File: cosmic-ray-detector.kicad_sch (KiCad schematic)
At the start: 51 parts, among them J1 15-91-0060, J2 15-91-0060, J3 SJ-43515RS-SMT, U1 LT3461, U2 LT1807, U3 Arduino_Nano_v3.x

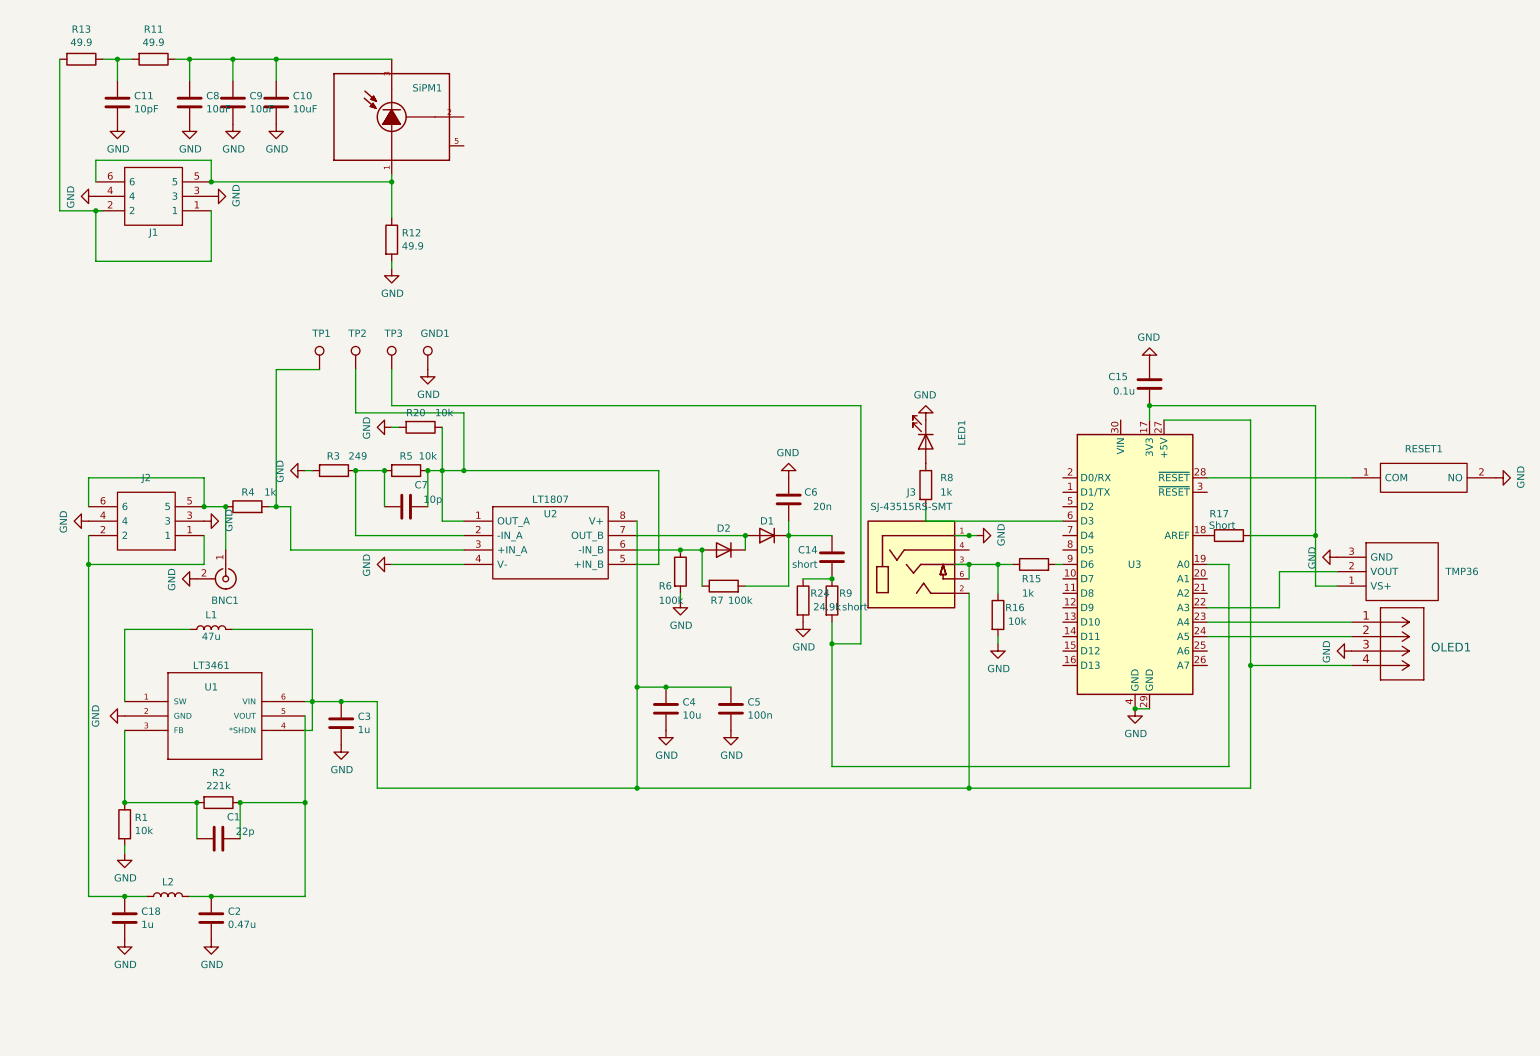
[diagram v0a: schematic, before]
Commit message: Add KiCad PCB project, CAD models, gerbers, libraries, and outputs
Track the full hardware project: KiCad schematic/PCB sources (v2 and
split variants), component libraries and 3D shapes, fabrication outputs
(gerbers, drill, position/BOM CSVs, STEP/STL/WRL), CAD enclosure models,
schematic exports (SVG/PDF), SPICE models, and reference photos.

Co-Authored-By: Claude Opus 4.8 <noreply@anthropic.com>
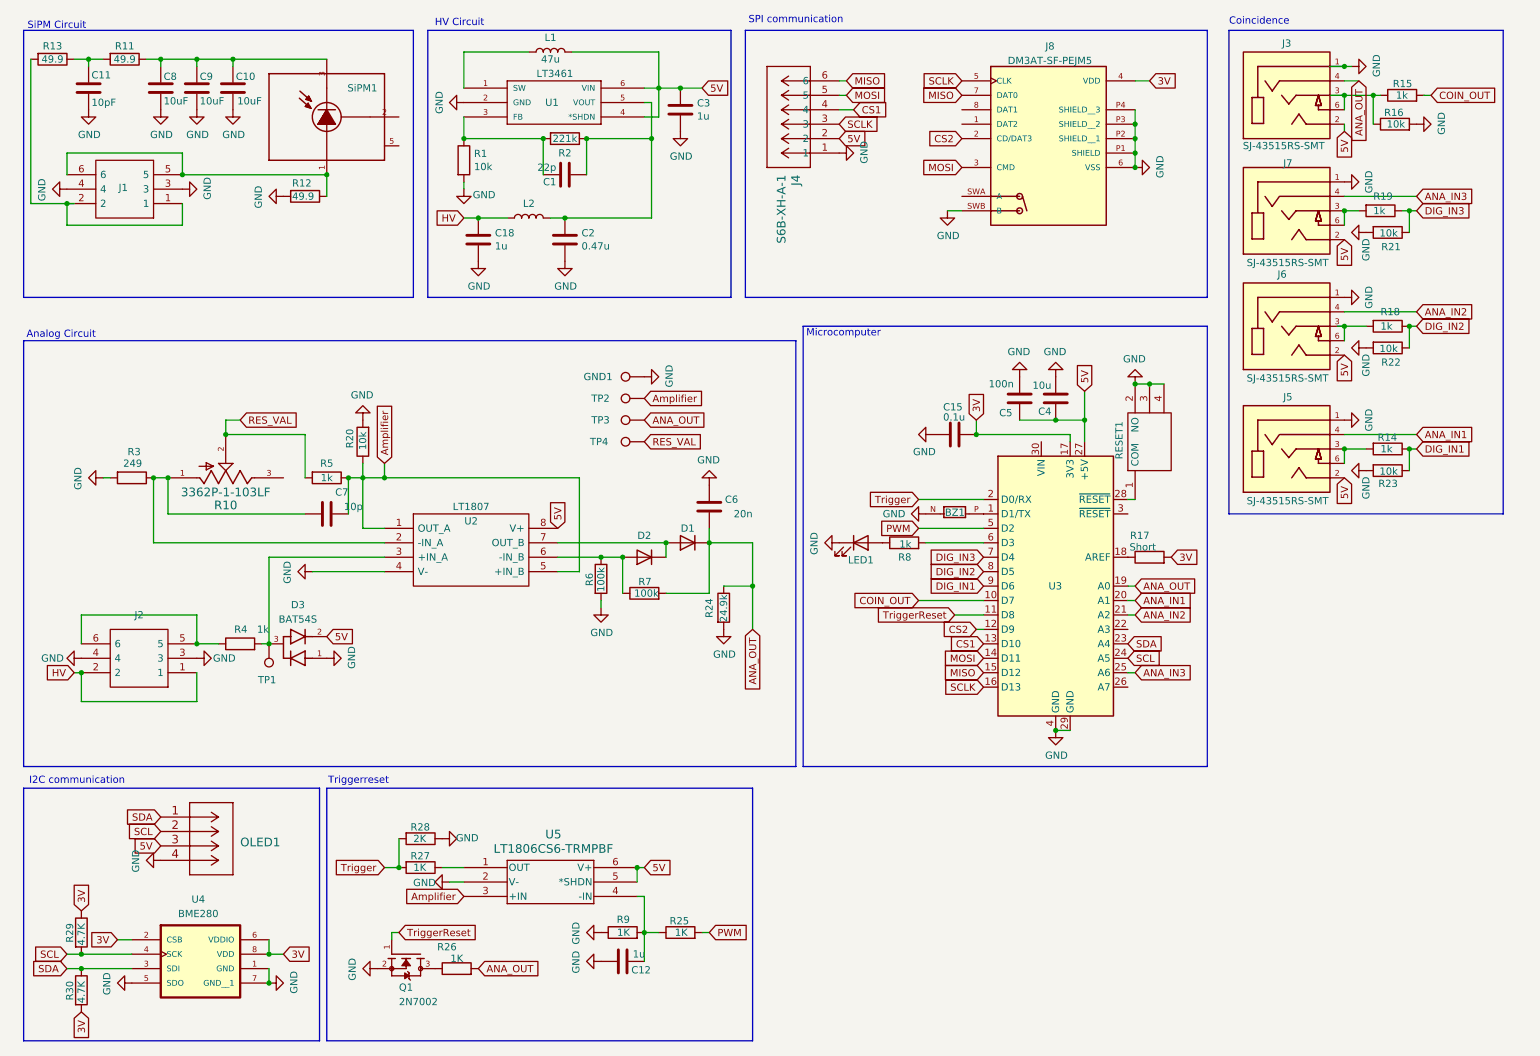
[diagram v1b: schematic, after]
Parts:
- removed BNC1: Conn_Coaxial, Connector_Coaxial:BNC_Amphenol_B6252HB-NPP3G-50_Horizontal, symbol Connector:Conn_Coaxial
- removed C14: short, Capacitor_SMD:C_0805_2012Metric, symbol Device:C
- removed TMP36: TMP36GT9Z, SamacSys_Parts:TO-92, symbol SamacSys_Parts:TMP36GT9Z
- added BZ1: CPT-1117-83-SMT-TR, SamacSys_Parts:XDCR_CPT-1117-83-SMT-TR, symbol CPT-1117-83-SMT-TR:CPT-1117-83-SMT-TR
- added C12: 1u, Capacitor_SMD:C_0805_2012Metric, symbol Device:C
- added D3: BAT54S, SamacSys_Parts:SOT95P240X120-3N, symbol cosmic-ray-detector:BAT54S
- added J4: S6B-XH-A-1, CONN_S6B-XH-A-1_JST, symbol cosmic-ray-detector:S6B-XH-A-1
- added J5, J6, J7: SJ-43515RS-SMT, cosmic-ray-detector:SJ-43515RS-SMT-TR, symbol SJ-43515RS-SMT:SJ-43515RS-SMT
- added J8: DM3AT-SF-PEJM5, cosmic-ray-detector:HRS_DM3AT-SF-PEJM5, symbol DM3AT-SF-PEJM5:DM3AT-SF-PEJM5
- added Q1: 2N7002, SamacSys_Parts:SOT95P240X111-3N, symbol cosmic-ray-detector:2N7002
- added R10: 3362P-1-103LF, SamacSys_Parts:TRIM_3362P-1-103LF, symbol cosmic-ray-detector:3362P-1-103LF
- added R14, R18, R19: 1k, Resistor_SMD:R_0805_2012Metric, symbol Device:R
- added R21, R22, R23: 10k, Resistor_SMD:R_0805_2012Metric, symbol Device:R
- added R25, R26, R27: 1K, Resistor_SMD:R_0805_2012Metric, symbol Device:R
- added R28: 2K, Resistor_SMD:R_0805_2012Metric, symbol Device:R
- added R29, R30: 4.7K, Resistor_SMD:R_0805_2012Metric, symbol Device:R
- added TP4: TestPoint, TestPoint:TestPoint_THTPad_3.0x3.0mm_Drill1.5mm, symbol Connector:TestPoint
- added U4: BME280, SamacSys_Parts:PSON65P250X250X100-8N, symbol cosmic-ray-detector:BME280
- added U5: LT1806CS6-TRMPBF, Package_TO_SOT_SMD:TSOT-23-6, symbol cosmic-ray-detector:LT1806CS6-TRMPBF
- GND1, TP1, TP2, TP3: footprint TestPoint:TestPoint_Keystone_5000-5004_Miniature -> TestPoint:TestPoint_THTPad_3.0x3.0mm_Drill1.5mm
- R5: value 10k -> 1k
- R9: value short -> 1K
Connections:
- net GND: now also OLED1.4, R9.1, RESET1.3, RESET1.4, BZ1.N, C12.2, D3.1, J4.1, J5.1, J6.1, J7.1, J8.6 (VSS), J8.P1 (SHIELD), J8.P2 (SHIELD__1), J8.P3 (SHIELD__2), J8.P4 (SHIELD__3), J8.SWB (B), Q1.2, R21.2, R22.2, R23.2, R28.1, U4.1 (GND), U4.5 (SDO), U4.7 (GND__1), U5.2 (V-); no longer OLED1.3
- net 5V: now reaches C3.1, C4.1, C5.1, J3.2, L1.2, U1.4 (*SHDN), U1.6 (VIN), U2.8 (V+), U3.27 (+5V)
- net 5V: now also OLED1.3, D3.2, J4.2, J5.2, J6.2, J7.2, U5.5 (*SHDN), U5.6 (V+); no longer OLED1.4
- net ANA_OUT: now reaches TP3.1, U3.19 (A0)
- net ANA_OUT: now also C6.1, D1.1 (K), J3.4, R24.1, R7.2, R26.2; no longer R9.2
- net Amplifier: now reaches C7.2, R20.1, R5.1, TP2.1, U2.1 (OUT_A), U2.5 (+IN_B)
- net Amplifier: now also U5.3 (+IN)
- net HV: now reaches C18.1, J2.1, J2.2, L2.1
- net COIN_OUT: now reaches R15.2
- net COIN_OUT: now also U3.10 (D7); no longer U3.9 (D6)
- net at C7.1, R3.1, U2.2 (-IN_A): now also R10.1; no longer R5.2
- net at R4.2, TP1.1, U2.3 (+IN_A): now also D3.3
- net at U3.1 (D1/TX): now also BZ1.P
- net TriggerReset: now reaches U3.11 (D8)
- net TriggerReset: now also Q1.1
- net CS2: now reaches U3.12 (D9)
- net CS2: now also J8.2 (CD/DAT3)
- net CS1: now reaches U3.13 (D10)
- net CS1: now also J4.4
- net MOSI: now reaches U3.14 (D11)
- net MOSI: now also J4.5, J8.3 (CMD)
- net MISO: now reaches U3.15 (D12)
- net MISO: now also J4.6, J8.7 (DAT0)
- net SCLK: now reaches U3.16 (D13)
- net SCLK: now also J4.3, J8.5 (CLK)
- net 3V: now reaches C15.1, R17.2, U3.17 (3V3)
- net 3V: now also J8.4 (VDD), R29.1, R30.2, U4.2 (CSB), U4.6 (VDDIO), U4.8 (VDD)
- net Trigger: now reaches U3.2 (D0/RX)
- net Trigger: now also R27.2, R28.2
- net ANA_IN1: now reaches U3.20 (A1)
- net ANA_IN1: now also J5.4
- net ANA_IN2: now reaches U3.21 (A2)
- net ANA_IN2: now also J6.4
- net SDA: now reaches OLED1.1, U3.23 (A4)
- net SDA: now also R30.1, U4.3 (SDI)
- net SCL: now reaches OLED1.2, U3.24 (A5)
- net SCL: now also R29.2, U4.4 (SCK)
- net ANA_IN3: now reaches U3.25 (A6)
- net ANA_IN3: now also J7.4
- net PWM: now reaches U3.5 (D2)
- net PWM: now also R25.2
- net DIG_IN3: now reaches U3.7 (D4)
- net DIG_IN3: now also R19.1, R21.1
- net DIG_IN2: now reaches U3.8 (D5)
- net DIG_IN2: now also R18.1, R22.1
- new net: J7.3, J7.6, R19.2
- new net: C12.1, R25.1, R9.2, U5.4 (-IN)
- new net: J6.3, J6.6, R18.2
- new net: R27.1, U5.1 (OUT)
- new net: J5.3, J5.6, R14.2
- new net: Q1.3, R26.1
- new net DIG_IN1: R14.1, R23.1, U3.9 (D6)
- new net RES_VAL: R10.2, R5.2, TP4.1
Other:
- note added: "Analog Circuit"
- note added: "Coincidence"
- note added: "HV Circuit"
- note added: "I2C communication"
- note added: "Microcomputer"
- note added: "SPI communication"
- note added: "SiPM Circuit"
- note added: "Triggerreset"
- moved on the sheet: C1, C10, C11, C15, C18, C2, C3, C4, C5, C6, C7, C8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
